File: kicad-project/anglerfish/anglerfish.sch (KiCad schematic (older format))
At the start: 32 parts, among them J1 Conn_01x34_MountingPin

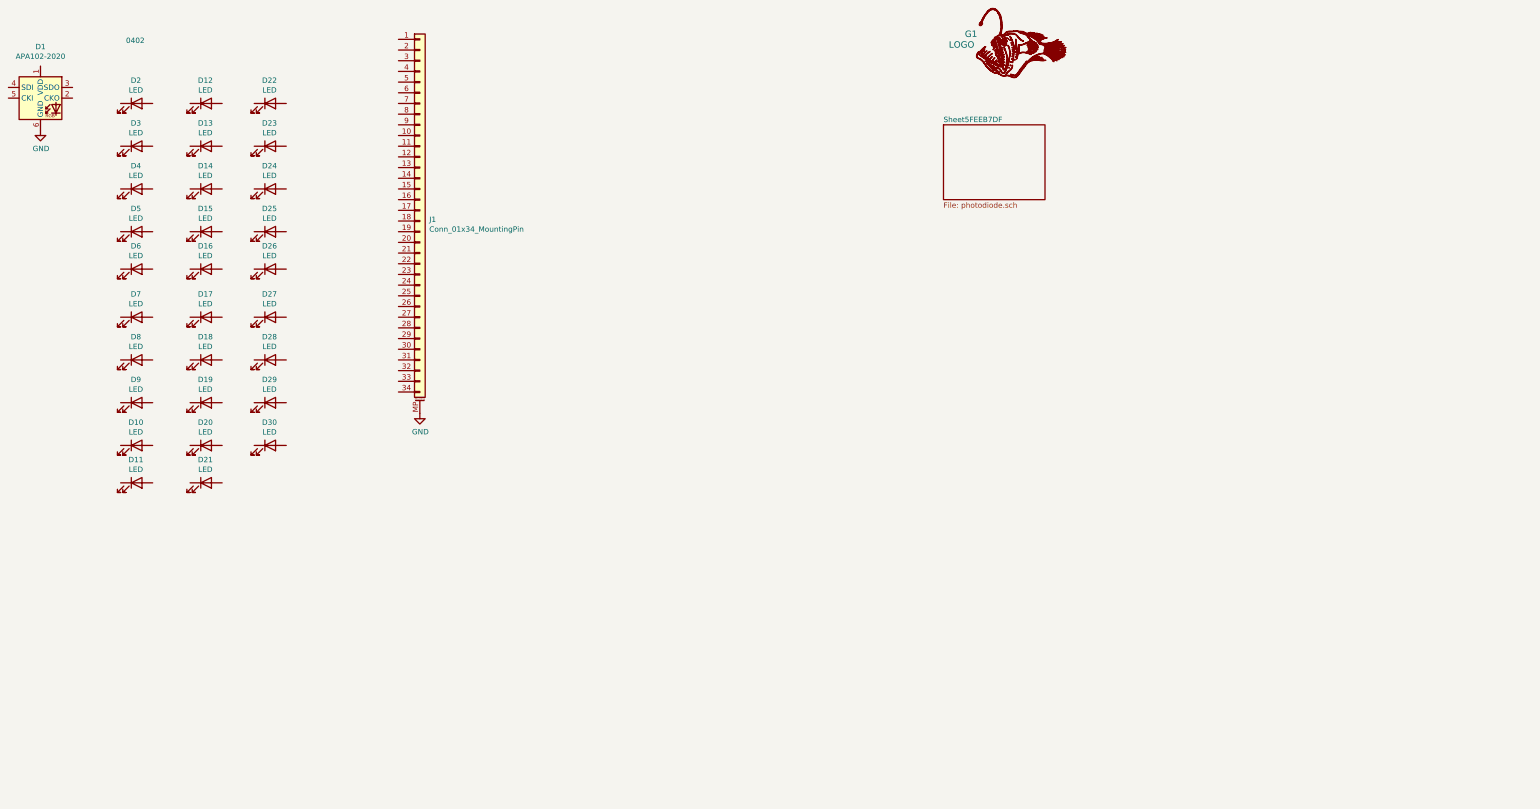
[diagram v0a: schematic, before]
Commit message: Schematic entered. Adding placing the resistors in the layout now.
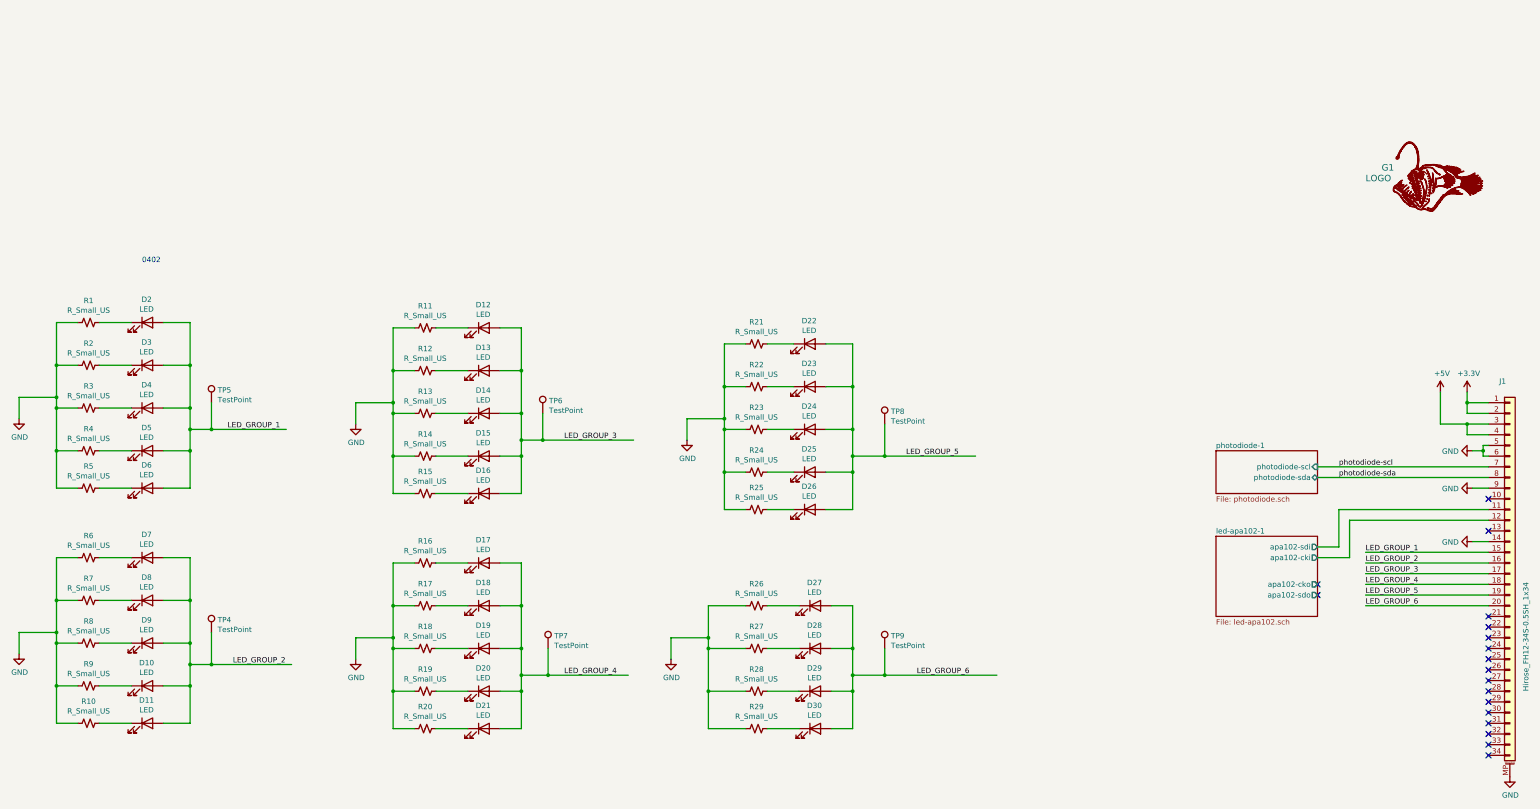
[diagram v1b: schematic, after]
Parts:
- removed D1: APA102-2020, LED_SMD:LED-APA102-2020, symbol LED:APA102-2020
- added R1, R10, R11, R12, R13, R14, R15, R16, R17, R18, R19, R2, R20, R21, R22, R23, R24, R25, R26, R27, R28, R29, R3, R4, R5, R6, R7, R8, R9: R_Small_US, Resistor_SMD:R_0402_1005Metric, symbol Device:R_Small_US
- added TP4, TP5, TP6, TP7, TP8, TP9: TestPoint, TestPoint:TestPoint_Pad_D1.5mm, symbol Connector:TestPoint
- J1: value Conn_01x34_MountingPin -> Hirose_FH12-34S-0.5SH_1x34
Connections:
- net labels added: +3.3V, +5V, LED_GROUP_1, LED_GROUP_2, LED_GROUP_3, LED_GROUP_4, LED_GROUP_5, LED_GROUP_6, photodiode-scl, photodiode-sda
- wire segments 0 -> 205
- no-connect marks 0 -> 18
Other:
- moved on the sheet: D10, D11, D12, D13, D14, D15, D16, D17, D18, D19, D2, D20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

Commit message: Finished routing. trying to generate a bom.
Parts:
- D10, D11, D12, D13, D14, D15, D16, D17, D18, D19, D2, D20, D21, D22, D23, D24, D25, D26, D27, D28, D29, D3, D30, D4, D5, D6, D7, D8, D9: LCSC Part (none) -> C130725

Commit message: Generated gerbers. I discovered that I was working in a temp folder, so I erased the files under the anglerfish folder and manually brought the files from the temp folder.
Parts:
- added TP10, TP11, TP12, TP13, TP14, TP15: TestPoint, TestPoint:TestPoint_Pad_D1.5mm, symbol Connector:TestPoint
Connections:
- net labels added: photodiode-int
- wire segments 205 -> 216
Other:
- note added: "All LED and Resistors are 0402.\nAll testpoints are TestPoint:TestPoint_Pad_D1.5mm.\nResistor values are TBD."
- note removed: "0402"
